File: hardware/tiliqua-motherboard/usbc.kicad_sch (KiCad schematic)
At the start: 8 parts, among them J7 USB_C_Receptacle_USB2.0_14P, U8 TUSB322I, U9 AP2161W

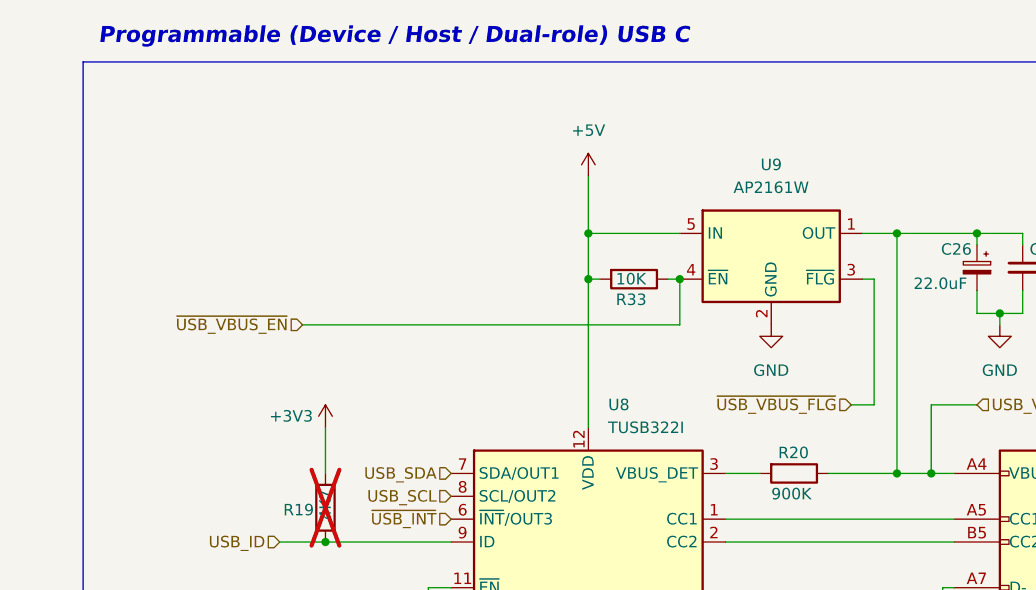
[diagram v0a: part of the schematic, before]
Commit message: place most parts
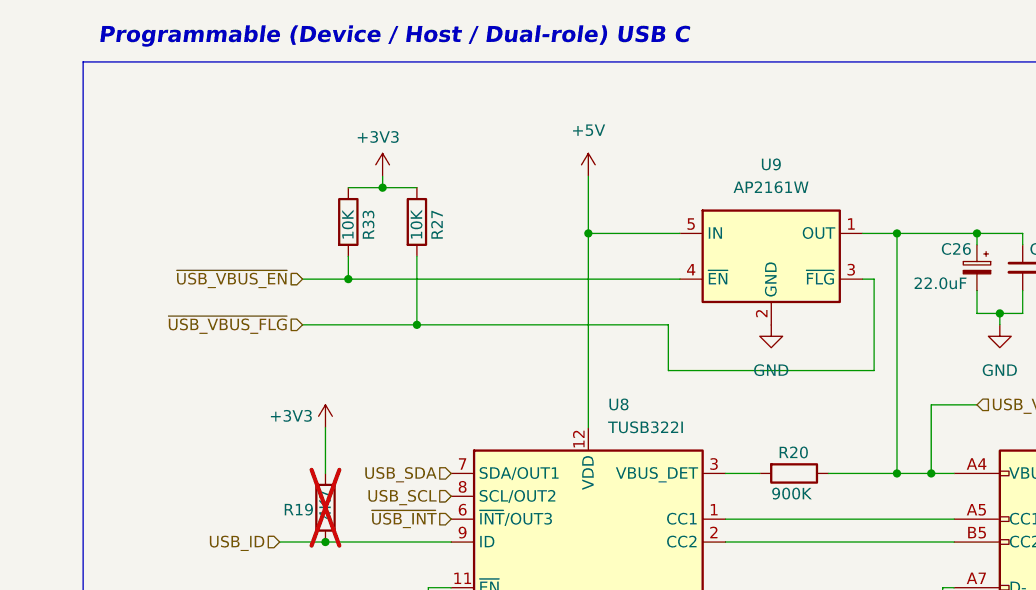
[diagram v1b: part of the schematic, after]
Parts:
- added R27: 10K, Resistor_SMD:R_0402_1005Metric, symbol Device:R
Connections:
- net +3V3: now also R33.1, R27.1
- net +5V: no longer R33.2
- net ~{USB_VBUS_EN}: now also R33.2; no longer R33.1
- net ~{USB_VBUS_FLG}: now also R27.2
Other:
- moved on the sheet: R33

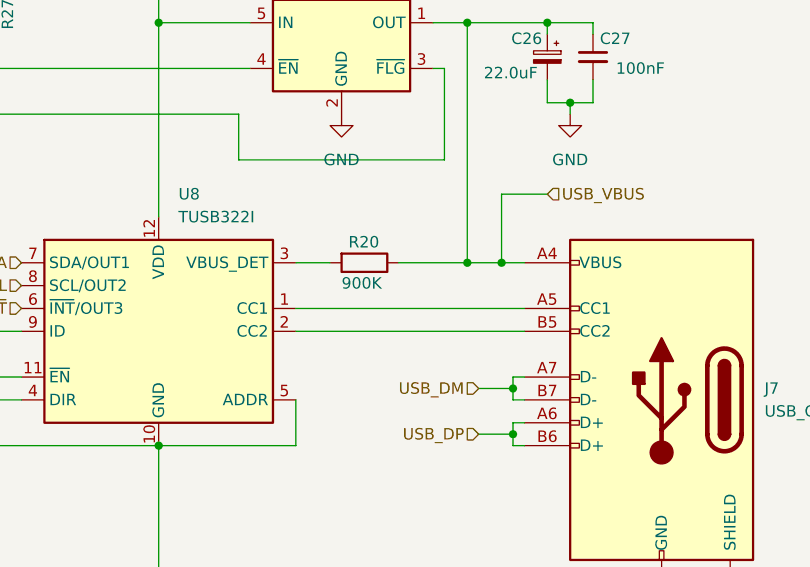
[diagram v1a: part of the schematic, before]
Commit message: add some part numbers
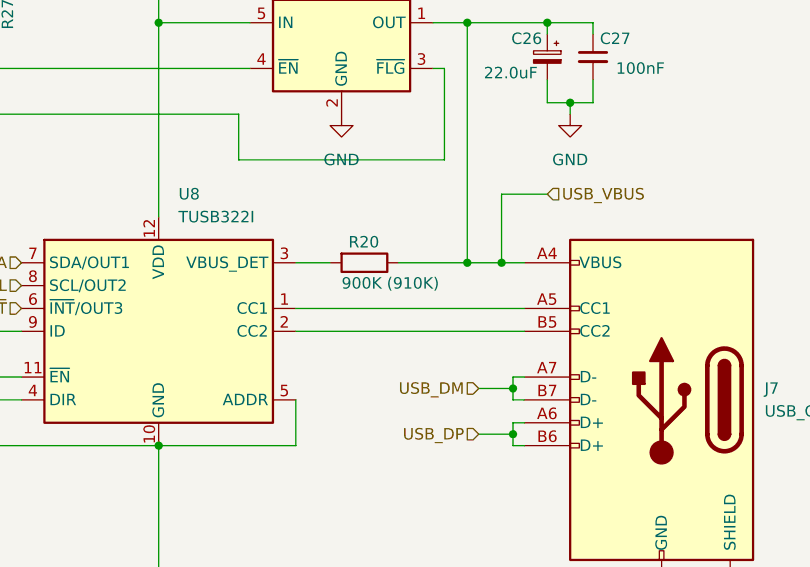
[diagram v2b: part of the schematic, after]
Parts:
- J7: lcsc# (none) -> C692526
- R20: value 900K -> 900K (910K); lcsc# (none) -> C25800
- R27, R33: lcsc# (none) -> C25744
- U8: lcsc# (none) -> C2674422
- U9: lcsc# (none) -> C176957
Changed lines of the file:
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@@
 			)
 		)
-		(property "Value" "900K"
+		(property "Value" "900K (910K)"
 			(at 167.64 83.566 90)
 			(effects
@@
 			)
 		)
-		(property "lcsc#" ""
+		(property "lcsc#" "C25800"
+			(at 170.18 81.28 0)
+			(effects
+				(font
+					(size 1.27 1.27)
+				)
+				(hide yes)
+			)
+		)
+		(property "Tol" ""
 			(at 170.18 81.28 0)
 			(effects
@@
 			)
 		)
+		(property "Tol" ""
+			(at 167.64 57.15 0)
+			(effects
+				(font
+					(size 1.27 1.27)
+				)
+				(hide yes)
+			)
+		)
+		(property "lcsc#" "C176957"
+			(at 167.64 57.15 0)
+			(effects
+				(font
+					(size 1.27 1.27)
+				)
+				(hide yes)
+			)
+		)
 		(pin "4"
 		)
@@
 			)
 		)
+		(property "Tol" ""
+			(at 118.11 85.09 0)
+			(effects
+				(font
+					(size 1.27 1.27)
+				)
+				(hide yes)
+			)
+		)
 		(pin "1"
 		)
@@
 			)
 		)
-		(property "lcsc#" ""
+		(property "lcsc#" "C25744"
+			(at 120.65 53.34 0)
+			(effects
+				(font
+					(size 1.27 1.27)
+				)
+				(hide yes)
+			)
+		)
+		(property "Tol" ""
 			(at 120.65 53.34 0)
 			(effects
@@
 			)
 		)
-		(property "lcsc#" ""
+		(property "lcsc#" "C25744"
+			(at 128.27 53.34 0)
+			(effects
+				(font
+					(size 1.27 1.27)
+				)
+				(hide yes)
+			)
+		)
+		(property "Tol" ""
 			(at 128.27 53.34 0)
 			(effects
@@
 		)
 		(property "mfg#" "C1608X7R1E104KT000N"
+			(at 195.58 58.42 0)
+			(effects
+				(font
+					(size 1.27 1.27)
+				)
+				(hide yes)
+			)
+		)
+		(property "Tol" ""
 			(at 195.58 58.42 0)
 			(effects
@@
 			)
 		)
+		(property "Tol" ""
+			(at 190.5 58.42 0)
+			(effects
+				(font
+					(size 1.27 1.27)
+				)
+				(hide yes)
+			)
+		)
 		(pin "1"
 		)
@@
 			)
 		)
+		(property "Tol" ""
+			(at 147.32 88.9 0)
+			(effects
+				(font
+					(size 1.27 1.27)
+				)
+				(hide yes)
+			)
+		)
+		(property "lcsc#" "C2674422"
+			(at 147.32 88.9 0)
+			(effects
+				(font
+					(size 1.27 1.27)
+				)
+				(hide yes)
+			)
+		)
 		(pin "11"
 		)
@@
 			(at 203.2 96.52 0)
 			(effects
+				(font
+					(size 1.27 1.27)
+				)
+				(hide yes)
+			)
+		)
+		(property "Tol" ""
+			(at 203.2 96.52 0)
+			(effects
+				(font
+					(size 1.27 1.27)
+				)
+				(hide yes)
+			)
+		)
+		(property "lcsc#" "C692526"
+			(at 203.2 96.52 0)
+			(effects

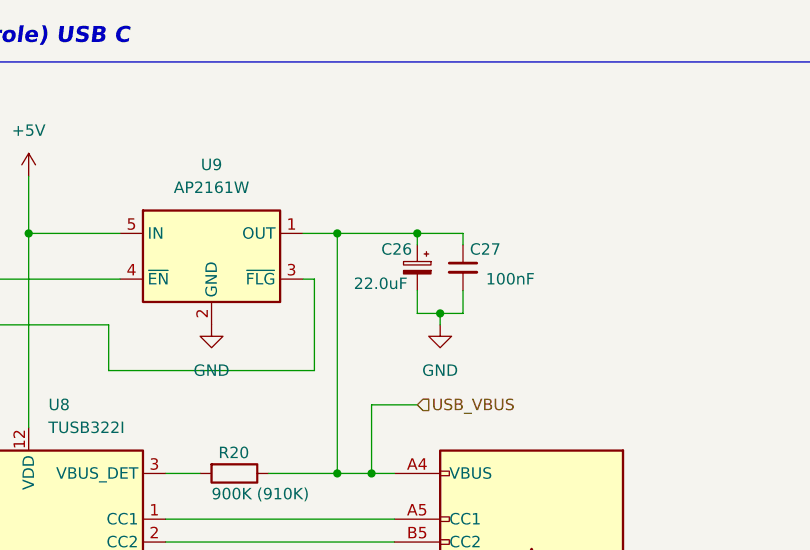
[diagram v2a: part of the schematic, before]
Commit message: hw/mobo-r3: swap tantalums for ceramics, clean up PSU routing, swap LDO for TPS7A91, add choke input capacitors
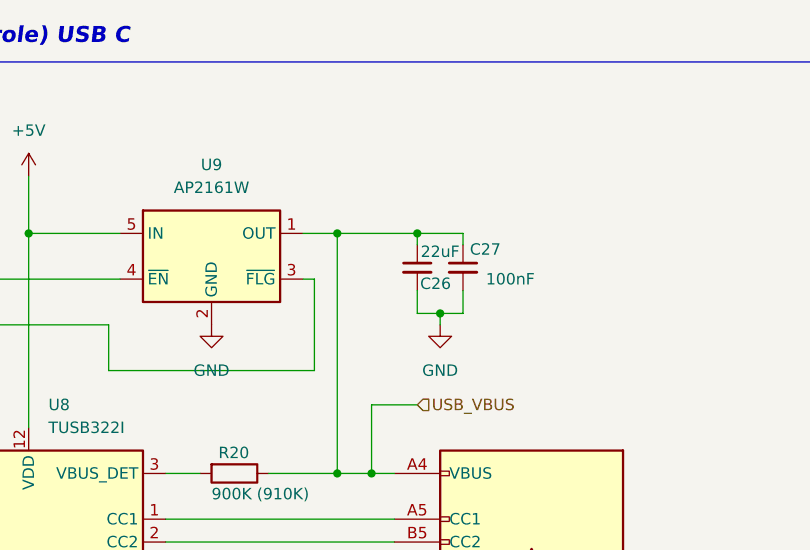
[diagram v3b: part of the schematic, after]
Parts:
- removed C26: 22.0uF, Capacitor_Tantalum_SMD:CP_EIA-3216-10_Kemet-I, symbol Device:C_Polarized_Small
- added C26: 22uF, Capacitor_SMD:C_1206_3216Metric, symbol Device:C_Small
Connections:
- net GND: now also C26.2
- net USB_VBUS: now also C26.1
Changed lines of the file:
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@@
+	)
+	(symbol
+		(lib_id "Device:C_Small")
+		(at 190.5 58.42 0)
+		(mirror y)
+		(unit 1)
+		(exclude_from_sim no)
+		(in_bom yes)
+		(on_board yes)
+		(dnp no)
+		(property "Reference" "C26"
+			(at 192.532 60.198 0)
+			(effects
+				(font
+					(size 1.27 1.27)
+				)
+			)
+		)
+		(property "Value" "22uF"
+			(at 193.04 56.642 0)
+			(effects
+				(font
+					(size 1.27 1.27)
+				)
+			)
+		)
+		(property "Footprint" "Capacitor_SMD:C_1206_3216Metric"
+			(at 190.5 58.42 0)
+			(effects
+				(font
+					(size 1.27 1.27)
+				)
+				(hide yes)
+			)
+		)
+		(property "Datasheet" "~"
+			(at 190.5 58.42 0)
+			(effects
+				(font
+					(size 1.27 1.27)
+				)
+				(hide yes)
+			)
+		)
+		(property "Description" "Unpolarized capacitor, small symbol"
+			(at 190.5 58.42 0)
+			(effects
+				(font
+					(size 1.27 1.27)
+				)
+				(hide yes)
+			)
+		)
+		(property "dig#" ""
+			(at 187.96 66.04 0)
+			(effects
+				(font
+					(size 1.27 1.27)
+				)
+				(hide yes)
+			)
+		)
+		(property "mfg#" " CL31A226KAHNNNE"
+			(at 187.96 68.58 0)
+			(effects
+				(font
+					(size 1.27 1.27)
+				)
+				(hide yes)
+			)
+		)
+		(property "lcsc#" "C12891"
+			(at 190.5 58.42 0)
+			(effects
+				(font
+					(size 1.27 1.27)
+				)
+				(hide yes)
+			)
+		)
+		(property "Tol" ""
+			(at 190.5 58.42 0)
+			(effects
+				(font
+					(size 1.27 1.27)
+				)
+				(hide yes)
+			)
+		)
+		(pin "1"
+		)
+		(pin "2"
+		)
+		(instances
+			(project "tiliqua-motherboard"
+				(path "/df6062c3-a570-4505-924c-c7fe32df3670/d2a2a9e8-d4aa-4c38-99cd-33ac9e017277"
+					(reference "C26")
+					(unit 1)
+				)
+			)
+		)
 	)
 	(symbol
@@
 					(unit 1)
 				)
-			)
-		)
-	)
-	(symbol
-		(lib_id "Device:C_Polarized_Small")
-		(at 190.5 58.42 0)
-		(mirror y)
-		(unit 1)
-		(exclude_from_sim no)
-		(in_bom yes)
-		(on_board yes)
-		(dnp no)
-		(property "Reference" "C26"
-			(at 188.214 56.388 0)
-			(effects
-				(font
-					(size 1.27 1.27)
-				)
-			)
-		)
-		(property "Value" "22.0uF"
-			(at 186.436 60.198 0)
-			(effects
-				(font
-					(size 1.27 1.27)
-				)
-			)
-		)
-		(property "Footprint" "Capacitor_Tantalum_SMD:CP_EIA-3216-10_Kemet-I"
-			(at 190.5 58.42 0)
-			(effects
-				(font
-					(size 1.27 1.27)
-				)
-				(hide yes)
-			)
-		)
-		(property "Datasheet" "~"
-			(at 190.5 58.42 0)
-			(effects
-				(font
-					(size 1.27 1.27)
-				)
-				(hide yes)
-			)
-		)
-		(property "Description" ""
-			(at 190.5 58.42 0)
-			(effects
-				(font
-					(size 1.27 1.27)
-				)
-				(hide yes)
-			)
-		)
-		(property "dig#" ""
-			(at 187.96 66.04 0)
-			(effects
-				(font
-					(size 1.27 1.27)
-				)
-				(hide yes)
-			)
-		)
-		(property "mfg#" "CA45-A-16V-22uF-K"
-			(at 187.96 68.58 0)
-			(effects
-				(font
-					(size 1.27 1.27)
-				)
-				(hide yes)
-			)
-		)
-		(property "lcsc#" "C782264"
-			(at 190.5 58.42 0)
-			(effects
-				(font
-					(size 1.27 1.27)
-				)
-				(hide yes)
-			)
-		)
-		(property "Tol" ""
-			(at 190.5 58.42 0)
-			(effects
-				(font
-					(size 1.27 1.27)
-				)
-				(hide yes)
-			)
-		)
-		(pin "1"
-		)
-		(pin "2"
-		)
-		(instances
-			(project "tiliqua-motherboard"
-				(path "/df6062c3-a570-4505-924c-c7fe32df3670/d2a2a9e8-d4aa-4c38-99cd-33ac9e017277"
-					(reference "C26")
-					(unit 1)
-				)

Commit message: hw/mobo-r3: add LCSC database / associations
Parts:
- C26: LCSC (none) -> C12891
- C27: LCSC (none) -> C14663
- J7: LCSC (none) -> C692526
- R19: LCSC (none) -> C25900
- R20: LCSC (none) -> C25800
- R27, R33: LCSC (none) -> C25744
- U8: LCSC (none) -> C2674422
- U9: LCSC (none) -> C176957
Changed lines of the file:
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@@
+			)
+		)
+		(property "LCSC" "C25800"
+			(at 168.402 78.994 0)
+			(effects
+				(font
+					(size 1.27 1.27)
+				)
+				(hide yes)
 			)
 		)
@@
 			)
 		)
+		(property "LCSC" "C176957"
+			(at 167.64 46.99 0)
+			(effects
+				(font
+					(size 1.27 1.27)
+				)
+				(hide yes)
+			)
+		)
 		(pin "4"
 		)
@@
 			)
 		)
+		(property "LCSC" "C25900"
+			(at 116.84 85.344 0)
+			(effects
+				(font
+					(size 1.27 1.27)
+				)
+				(hide yes)
+			)
+		)
 		(pin "1"
 		)
@@
 			)
 		)
+		(property "LCSC" "C12891"
+			(at 192.532 60.198 0)
+			(effects
+				(font
+					(size 1.27 1.27)
+				)
+				(hide yes)
+			)
+		)
 		(pin "1"
 		)
@@
 		(property "Tol" ""
 			(at 120.65 53.34 0)
+			(effects
+				(font
+					(size 1.27 1.27)
+				)
+				(hide yes)
+			)
+		)
+		(property "LCSC" "C25744"
+			(at 122.936 55.372 0)
 			(effects
 				(font
@@
 			)
 		)
+		(property "LCSC" "C25744"
+			(at 130.556 55.372 0)
+			(effects
+				(font
+					(size 1.27 1.27)
+				)
+				(hide yes)
+			)
+		)
 		(pin "1"
 		)
@@
 		(property "Tol" ""
 			(at 195.58 58.42 0)
+			(effects
+				(font
+					(size 1.27 1.27)
+				)
+				(hide yes)
+			)
+		)
+		(property "LCSC" "C14663"
+			(at 196.342 56.388 0)
 			(effects
 				(font
@@
 			)
 		)
+		(property "LCSC" "C2674422"
+			(at 149.5141 73.66 0)
+			(effects
+				(font
+					(size 1.27 1.27)
+				)
+				(hide yes)
+			)
+		)
 		(pin "11"
 		)
@@
 			(effects
 				(font
+					(size 1.27 1.27)
+				)
+				(hide yes)
+			)
+		)
+		(property "LCSC" "C692526"
+			(at 214.63 95.2499 0)
+			(effects
+				(font
